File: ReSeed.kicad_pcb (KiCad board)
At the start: 2 copper layers, 60.8 x 99.9 mm, 47 parts, among them CN1 EDGE_CONNECTOR, CN2 AUDIO_OUT, CN3 AUDIO_IN, CN4 DB9_MALE, Q1 2SC1815, SW1 SW_DIGIFIX, U1 MOS_8580, U2 CD4520BE, U3 74LS245, U4 GAL16V8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

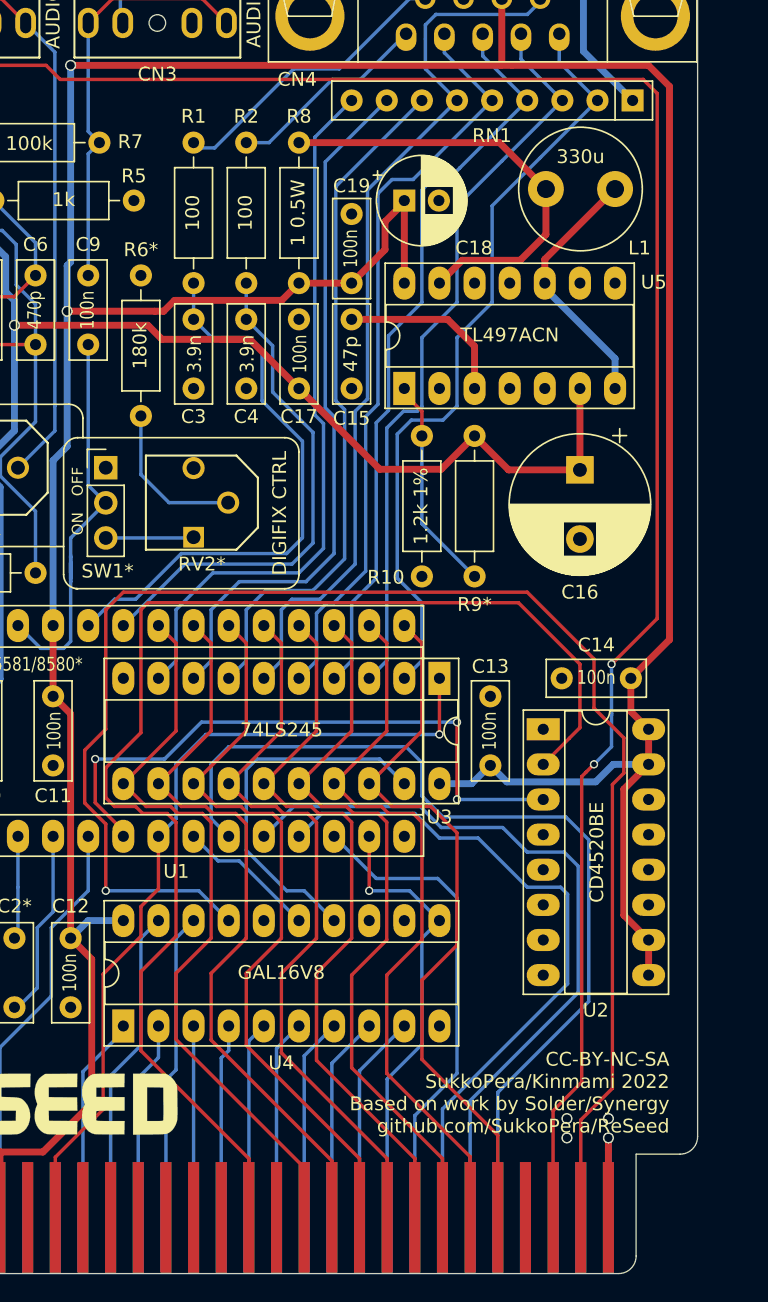
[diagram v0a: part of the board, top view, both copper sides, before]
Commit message: Add clock delay circuit See https://plus4world.powweb.com/forum/45294 for more information
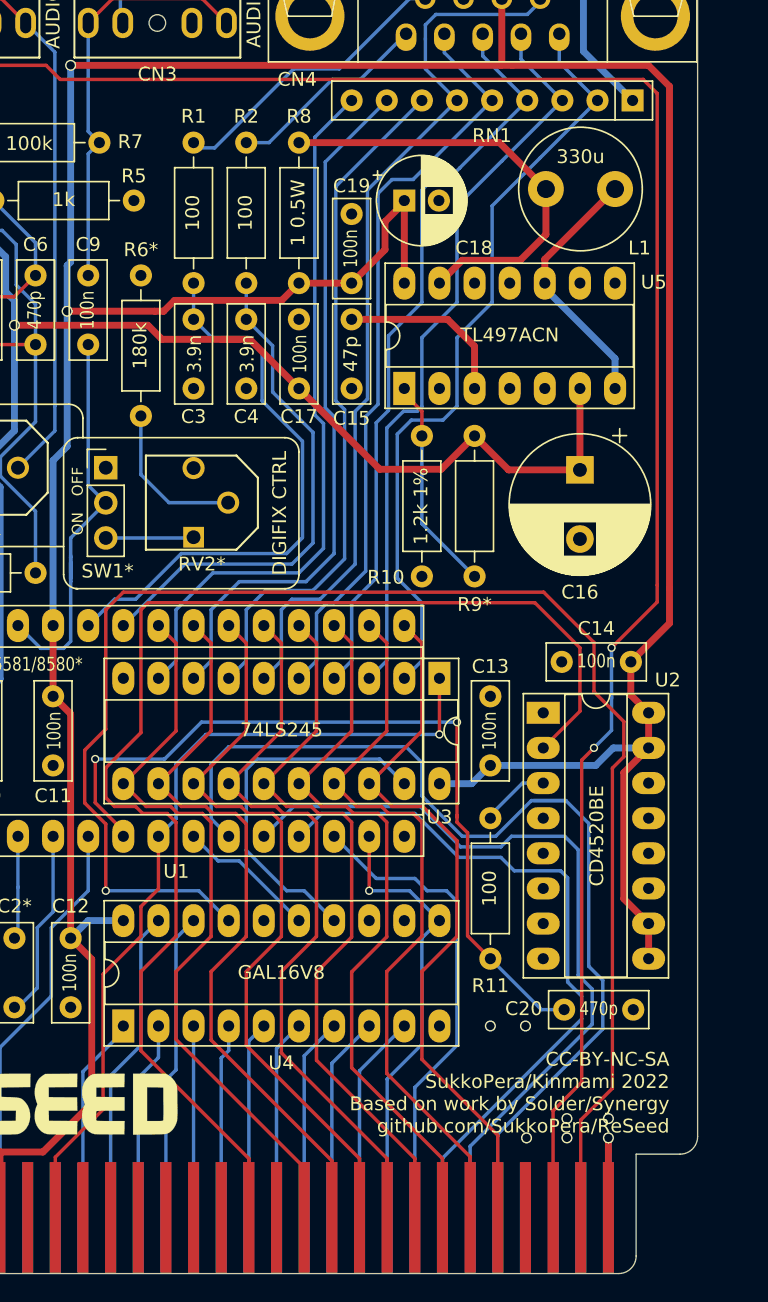
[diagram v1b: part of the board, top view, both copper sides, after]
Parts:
- added C20: 470p, Capacitor_THT:C_Disc_D7.0mm_W2.5mm_P5.00mm, F.Cu at (173.0, 129.0)
- added R11: 100, Resistor_THT:R_Axial_DIN0207_L6.3mm_D2.5mm_P10.16mm_Horizontal, F.Cu at (167.6, 125.3)
- Q1: value 2SC1815 -> BC549C
- moved C14 1.19 mm to (177.8, 103.8)
- moved U2 1.19 mm to (171.5, 107.5)
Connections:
- CN1 pad 10: Net-(CN1-Pad10) -> (no net)
- CN1 pad 11: Net-(CN1-Pad11) -> (no net)
- CN1 pad 13: Net-(CN1-Pad13) -> (no net)
- CN1 pad 22: Net-(CN1-Pad22) -> (no net)
- CN1 pad 4: Net-(CN1-Pad4) -> (no net)
- CN1 pad 6: Net-(CN1-Pad6) -> (no net)
- CN1 pad 7: Net-(CN1-Pad7) -> (no net)
- CN1 pad 8: Net-(CN1-Pad8) -> (no net)
- CN1 pad 9: Net-(CN1-Pad9) -> (no net)
- CN1 pad AA: Net-(CN1-PadAA) -> (no net)
- CN1 pad B: Net-(CN1-PadB) -> (no net)
- CN1 pad BB: Net-(CN1-PadBB) -> (no net)
- CN1 pad D: Net-(CN1-PadD) -> (no net)
- CN1 pad E: Net-(CN1-PadE) -> (no net)
- CN1 pad Z: Net-(CN1-PadZ) -> (no net)
- CN2 pad RN: Net-(CN2-PadRN) -> (no net)
- CN3 pad RN: Net-(CN3-PadRN) -> (no net)
- RV2 pad 3: Net-(RV2-Pad3) -> (no net)
- SW1 pad 1: Net-(SW1-Pad1) -> (no net)
- U1 pad 6: /half_mux -> /sidclk
- U2 pad 11: Net-(U2-Pad11) -> (no net)
- U2 pad 12: Net-(U2-Pad12) -> (no net)
- U2 pad 13: Net-(U2-Pad13) -> (no net)
- U2 pad 14: Net-(U2-Pad14) -> (no net)
- U2 pad 3: /half_mux -> Net-(R11-Pad2)
- U2 pad 4: Net-(U2-Pad4) -> (no net)
- U2 pad 5: Net-(U2-Pad5) -> (no net)
- U2 pad 6: Net-(U2-Pad6) -> (no net)
- U4 pad 12: Net-(U4-Pad12) -> (no net)
- U4 pad 13: Net-(U4-Pad13) -> (no net)
- U4 pad 16: Net-(U4-Pad16) -> (no net)
- U5 pad 11: Net-(U5-Pad11) -> (no net)
- U5 pad 12: Net-(U5-Pad12) -> (no net)
- U5 pad 9: Net-(U5-Pad9) -> (no net)
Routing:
- net /sidclk: track 0.00 -> 58.8 mm, vias 0 -> 2
- net /half_mux: track 45.5 -> 0.00 mm, vias 3 -> 0
- net /a0: track 67.8 -> 73.8 mm
- net Net-(R11-Pad2): track 0.00 -> 5.00 mm
- net /a1: track 54.1 -> 56.2 mm
- net /a2: track 49.7 -> 51.2 mm
- net +5V: track 284.7 -> 283.4 mm
- net /phi2: track 111.8 -> 112.5 mm
- net GND: vias 6 -> 9
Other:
- board text added: "V2"
- board text removed: "V1"

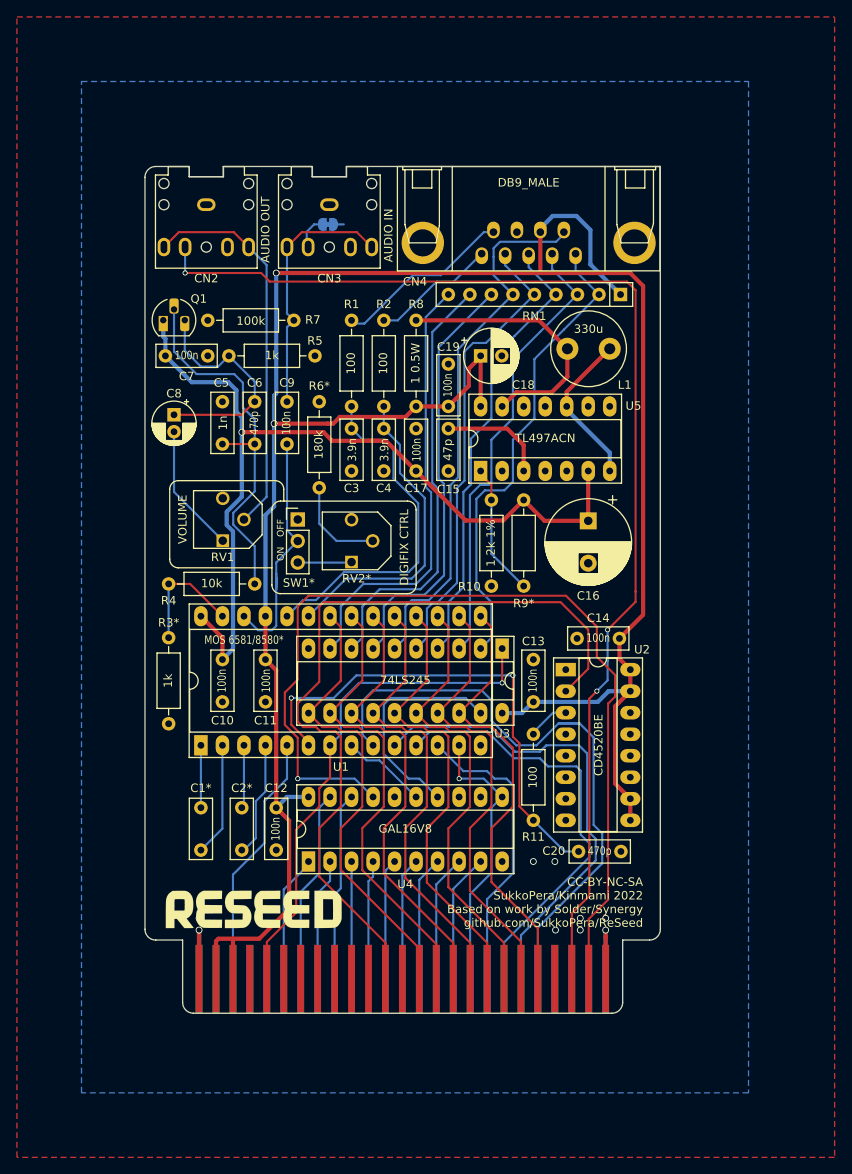
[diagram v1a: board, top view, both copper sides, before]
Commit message: Reset the 4520 with /RESET This required a lot of shuffling of the GAL pins.
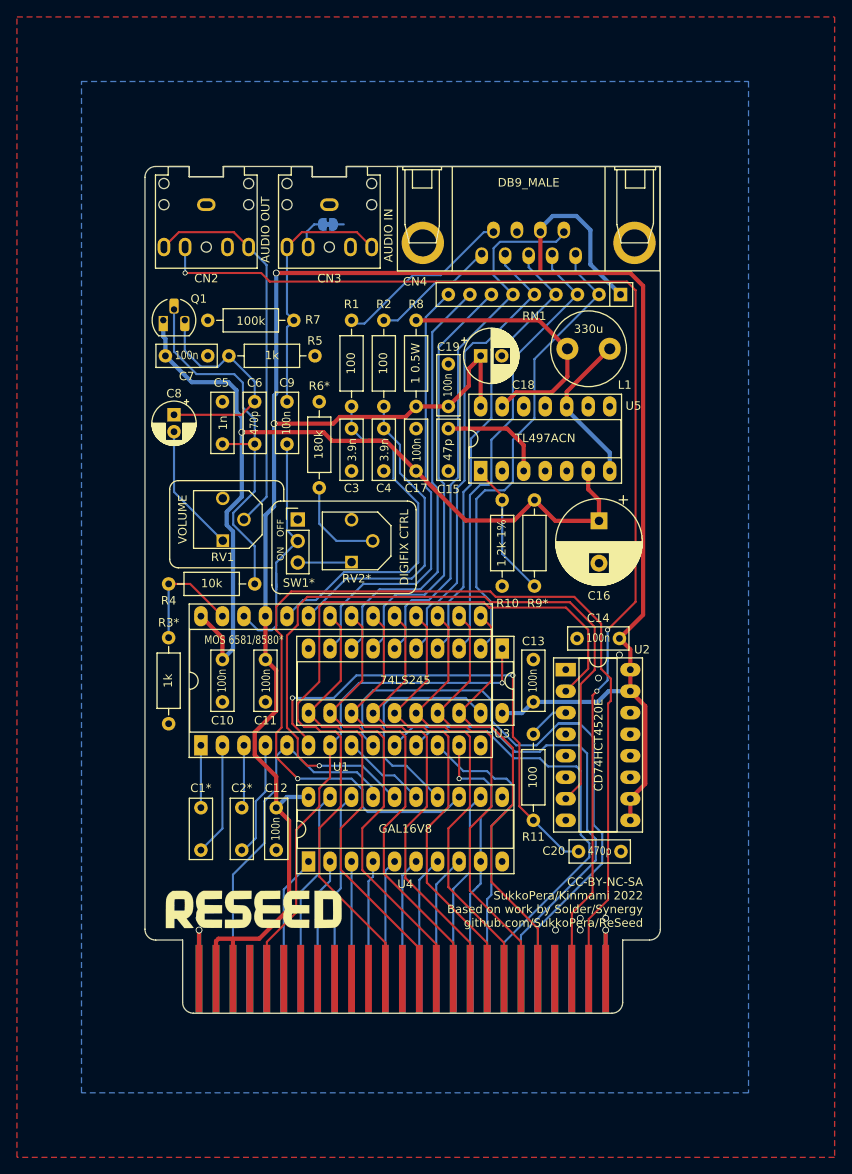
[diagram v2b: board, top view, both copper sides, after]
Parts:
- U2: value CD4520BE -> CD74HCT4520E
- moved C16 1.27 mm to (175.4, 90.0)
- moved R10 1.27 mm to (164.0, 97.7)
- moved R9 1.27 mm to (167.8, 97.7)
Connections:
- U2 pad 7: GND -> /reset
- U4 pad 11: /a4 -> (no net)
- U4 pad 12: (no net) -> /a5
- U4 pad 13: (no net) -> /phi2
- U4 pad 16: (no net) -> /reset
- U4 pad 17: /phi2 -> /~reset
- U4 pad 9: /a5 -> /a4
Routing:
- net /reset: track 0.00 -> 90.8 mm, vias 0 -> 1
- net /phi2: track 112.5 -> 128.6 mm
- net /~reset: track 30.2 -> 43.5 mm
- net /a5: track 15.2 -> 22.8 mm
- net +5V: track 283.4 -> 285.5 mm
- net +9V: track 109.2 -> 111.0 mm
- net /audio_in: track 31.6 -> 30.0 mm
- net /a4: track 32.9 -> 31.9 mm
- net Net-(R10-Pad2): track 15.4 -> 16.2 mm

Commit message: Add series resistors on joystick port
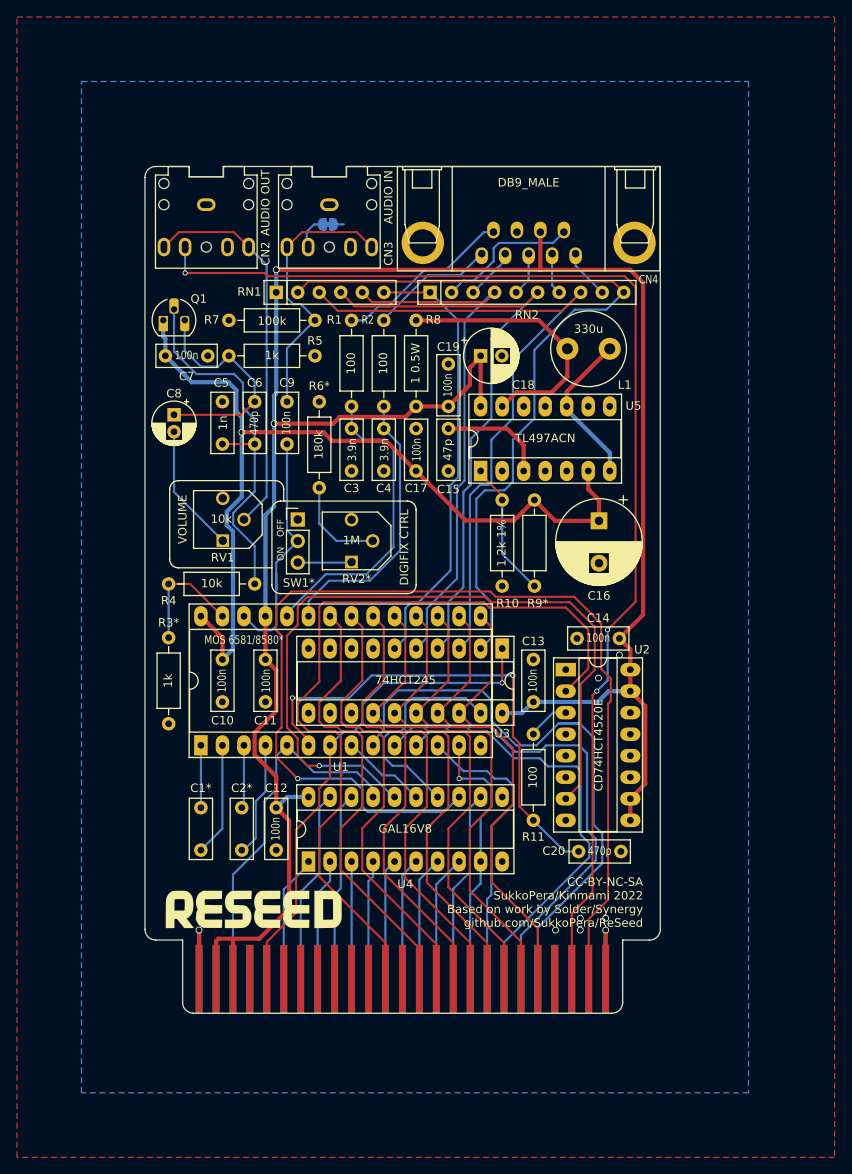
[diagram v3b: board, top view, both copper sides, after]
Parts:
- added RN2: 100, Resistor_THT:R_Array_SIP10, F.Cu at (155.4, 63.0)
- RN1: footprint Resistor_THT:R_Array_SIP9 -> Resistor_THT:R_Array_SIP6
- U3: value 74LS245 -> 74HCT245
- moved RN1 40.6 mm to (137.3, 63.0), turned to 0 degrees
- moved R7 2.49 mm to (131.7, 66.3)
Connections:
- RN1 pad 2: Net-(CN4-Pad1) -> Net-(RN1-Pad2)
- RN1 pad 3: Net-(CN4-Pad2) -> Net-(RN1-Pad3)
- RN1 pad 4: Net-(CN4-Pad3) -> Net-(RN1-Pad4)
- RN1 pad 5: Net-(CN4-Pad4) -> Net-(RN1-Pad5)
- RN1 pad 6: Net-(CN4-Pad6) -> Net-(RN1-Pad6)
- U3 pad 11: /d7 -> GND
- U3 pad 12: /d6 -> GND
- U3 pad 13: /d5 -> GND
- U3 pad 2: Net-(CN4-Pad1) -> Net-(RN1-Pad2)
- U3 pad 3: Net-(CN4-Pad2) -> Net-(RN1-Pad3)
- U3 pad 4: Net-(CN4-Pad3) -> Net-(RN1-Pad4)
- U3 pad 5: Net-(CN4-Pad4) -> Net-(RN1-Pad5)
- U3 pad 6: Net-(CN4-Pad6) -> Net-(RN1-Pad6)
- U3 pad 7: Net-(RN1-Pad7) -> GND
- U3 pad 8: Net-(RN1-Pad8) -> GND
- U3 pad 9: Net-(RN1-Pad9) -> GND
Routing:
- net Net-(RN1-Pad2): track 0.00 -> 93.6 mm
- net Net-(RN1-Pad3): track 0.00 -> 81.6 mm
- net Net-(RN1-Pad4): track 0.00 -> 71.5 mm
- net Net-(RN1-Pad5): track 0.00 -> 62.6 mm
- net Net-(RN1-Pad6): track 0.00 -> 52.6 mm
- net Net-(RN1-Pad9): track 51.7 -> 0.00 mm
- net Net-(RN1-Pad8): track 50.9 -> 0.00 mm
- net Net-(CN4-Pad1): track 56.4 -> 5.87 mm
- net Net-(RN1-Pad7): track 50.1 -> 0.00 mm
- net Net-(CN4-Pad2): track 54.5 -> 4.92 mm
- net Net-(CN4-Pad4): track 55.0 -> 6.14 mm
- net Net-(CN4-Pad3): track 54.0 -> 5.18 mm
- net Net-(CN4-Pad6): track 64.5 -> 16.6 mm
- net +5V: track 285.5 -> 268.7 mm
- net Net-(C3-Pad1): track 41.3 -> 36.4 mm
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
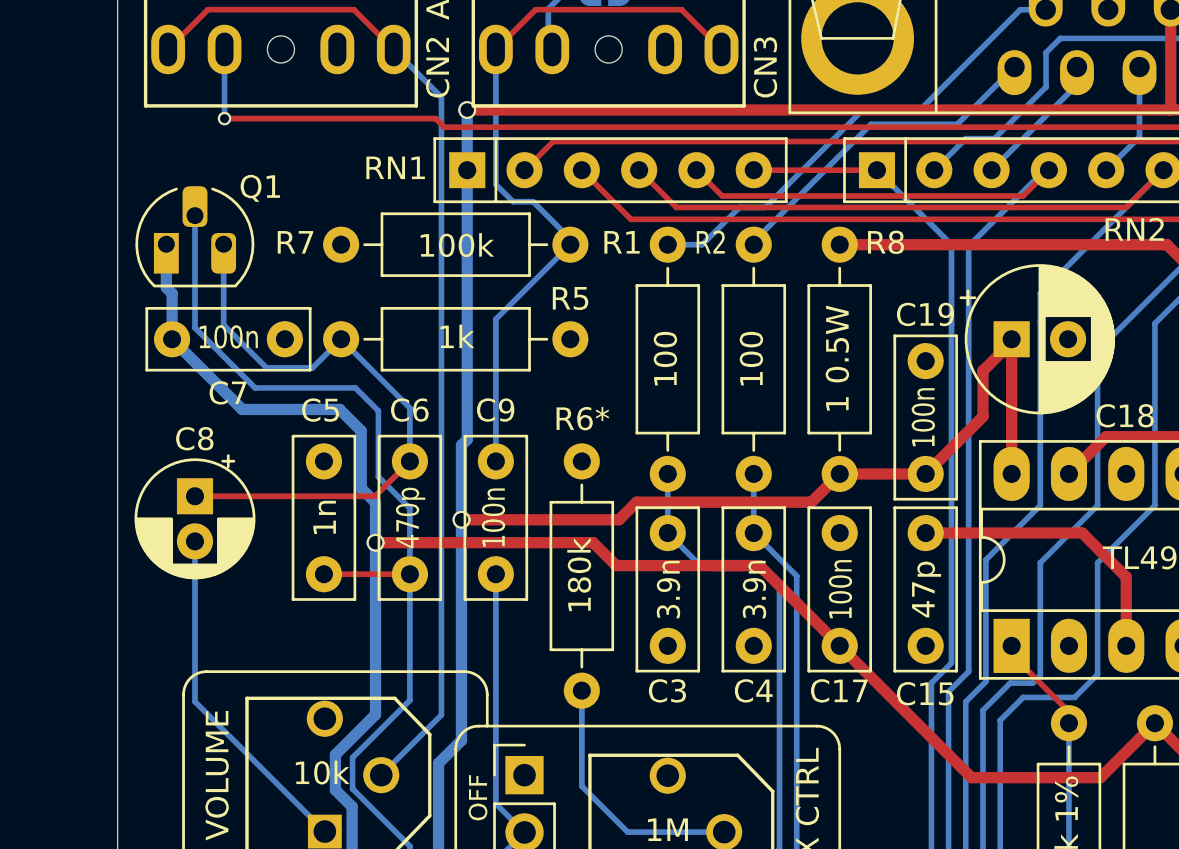
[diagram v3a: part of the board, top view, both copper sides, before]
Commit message: Improve positioning of some tracks/components/labels
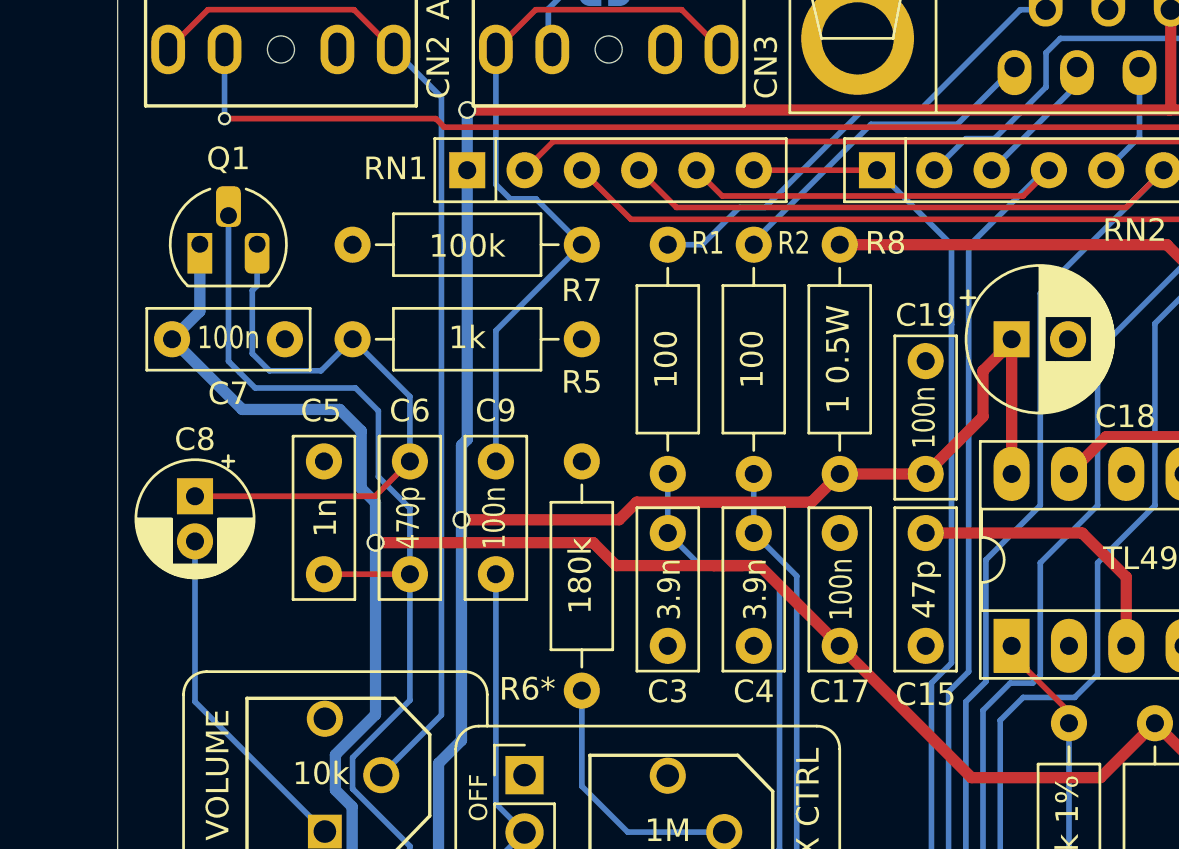
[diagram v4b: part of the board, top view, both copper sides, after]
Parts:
- moved Q1 1.48 mm to (125.4, 66.3)
- moved R5 0.51 mm to (142.4, 70.5)
- moved R7 0.51 mm to (132.2, 66.3)
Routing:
- net Net-(C6-Pad1): track 26.9 -> 27.6 mm
- net Net-(C5-Pad1): track 44.9 -> 44.3 mm
- net Net-(C9-Pad1): track 33.0 -> 33.5 mm
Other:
- board text added: "B"
- board text added: "C"
- board text added: "E"
